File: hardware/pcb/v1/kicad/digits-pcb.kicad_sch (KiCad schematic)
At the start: 19 parts, among them J1 Conn_02x20_Odd_Even, J10 Conn_01x02, J2 Conn_01x03, J3 Barrel_Jack_Switch, J4 Conn_01x07, J5 Conn_01x04, J6 Conn_01x02, J7 Screw_Terminal_01x02, J8 Conn_01x04, J9 Conn_01x03, SW1 SW_Push, U1 LM2596S-5

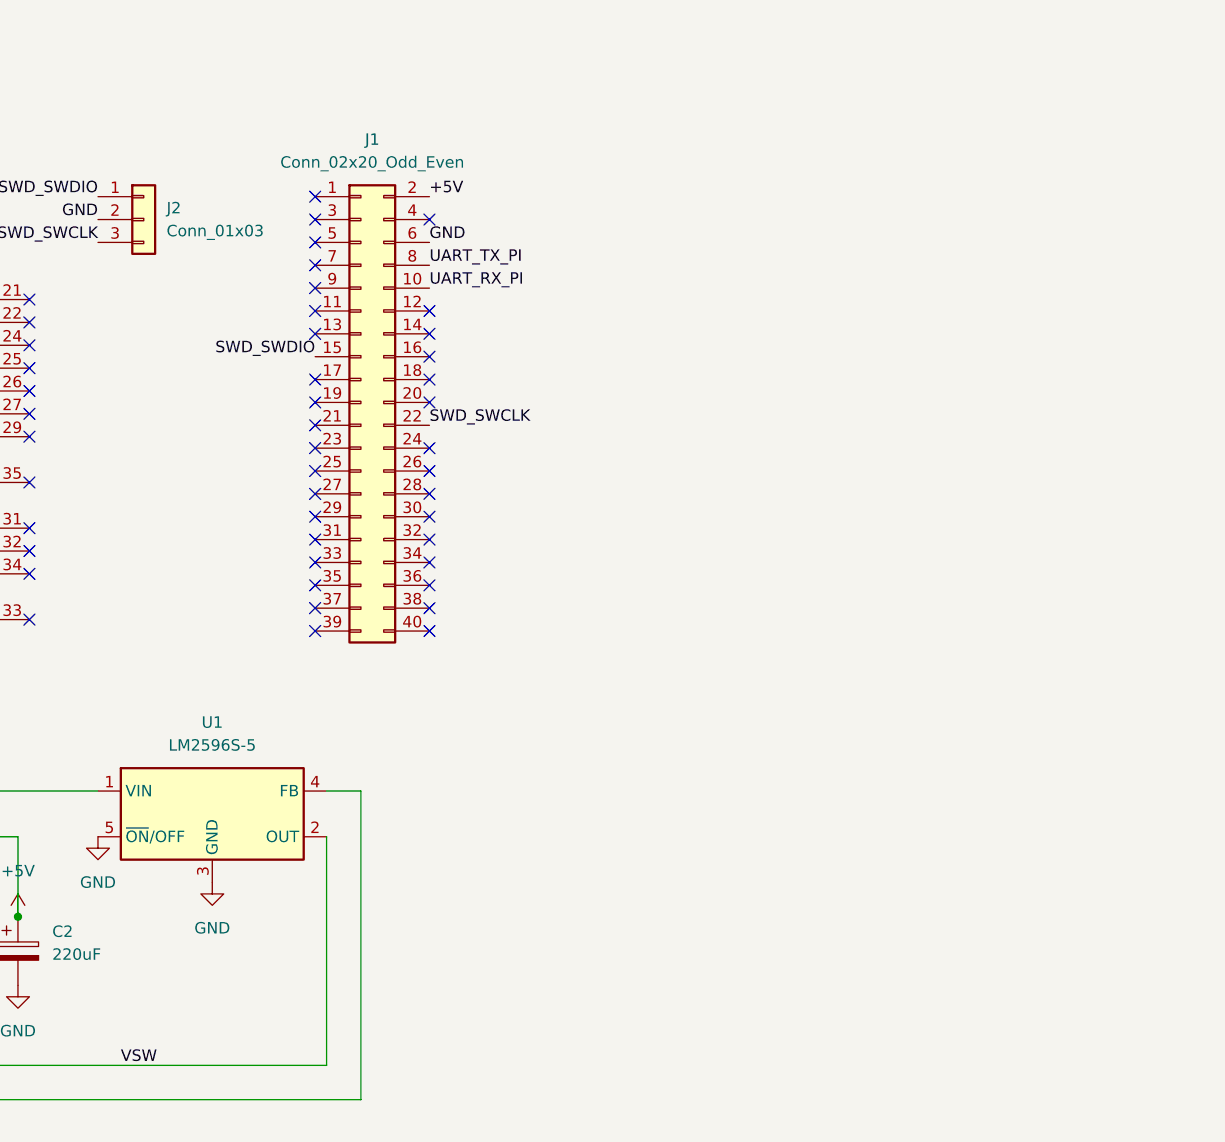
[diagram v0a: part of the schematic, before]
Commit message: feat(hardware): v1.1 design in progress — codec header + audit follow-ups
Schematic (via subagents + manual):
- Add J_CODEC (2x20 female, Conn_02x20_Odd_Even) for the Codec Zero HAT to
  plug into directly via its factory 40-pin receptacle
- Add global labels linking J1 <-> J_CODEC for the 8 audio + power signals:
  CODEC_SDA, CODEC_SCL, CODEC_BCLK, CODEC_WCLK, CODEC_DIN, CODEC_DOUT, plus
  +3V3 and GND
- Add HAT_ID_SD / HAT_ID_SC labels on J1 pins 27/28 and J_CODEC pins 27/28
  so the Pi bootloader can auto-detect the HAT via its on-board EEPROM
- No_connect flags on unused J_CODEC pins

ERRATA.md:
- Annotate v1.1 resolution status for each of the 5 pre-existing errata
  items. #1 (switching node) marked APPLIED; #2-5 marked PENDING for v1.1
- Add introductory note that the design files in this directory are now
  evolving toward v1.1

PCB (WIP):
- Initial placement tweaks; full routing of J_CODEC + resolution of the
  other errata items is in progress
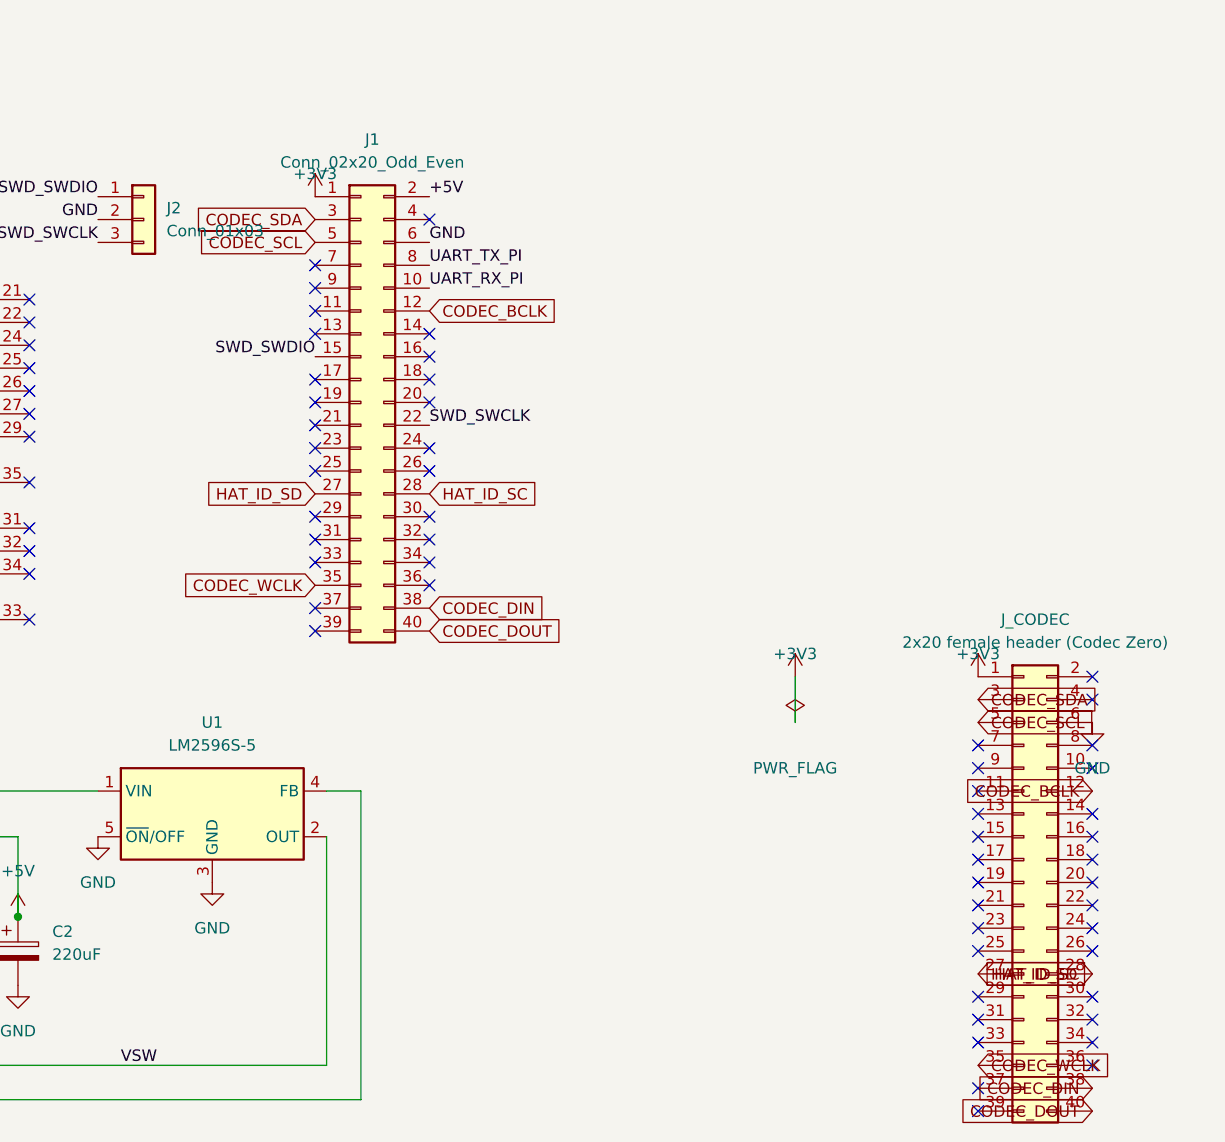
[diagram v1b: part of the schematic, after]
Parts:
- added J_CODEC: 2x20 female header (Codec Zero), Connector_PinHeader_2.54mm:PinHeader_2x20_P2.54mm_Vertical, symbol Connector_Generic:Conn_02x20_Odd_Even
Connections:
- net GND: now also J_CODEC.6 (Pin_6)
- net +3V3: now reaches J1.1 (Pin_1)
- net +3V3: now also J_CODEC.1 (Pin_1)
- net CODEC_BCLK: now reaches J1.12 (Pin_12)
- net CODEC_BCLK: now also J_CODEC.12 (Pin_12)
- net HAT_ID_SD: now reaches J1.27 (Pin_27)
- net HAT_ID_SD: now also J_CODEC.27 (Pin_27)
- net HAT_ID_SC: now reaches J1.28 (Pin_28)
- net HAT_ID_SC: now also J_CODEC.28 (Pin_28)
- net CODEC_SDA: now reaches J1.3 (Pin_3)
- net CODEC_SDA: now also J_CODEC.3 (Pin_3)
- net CODEC_WCLK: now reaches J1.35 (Pin_35)
- net CODEC_WCLK: now also J_CODEC.35 (Pin_35)
- net CODEC_DIN: now reaches J1.38 (Pin_38)
- net CODEC_DIN: now also J_CODEC.38 (Pin_38)
- net CODEC_DOUT: now reaches J1.40 (Pin_40)
- net CODEC_DOUT: now also J_CODEC.40 (Pin_40)
- net CODEC_SCL: now reaches J1.5 (Pin_5)
- net CODEC_SCL: now also J_CODEC.5 (Pin_5)
- no-connect marks 54 -> 75

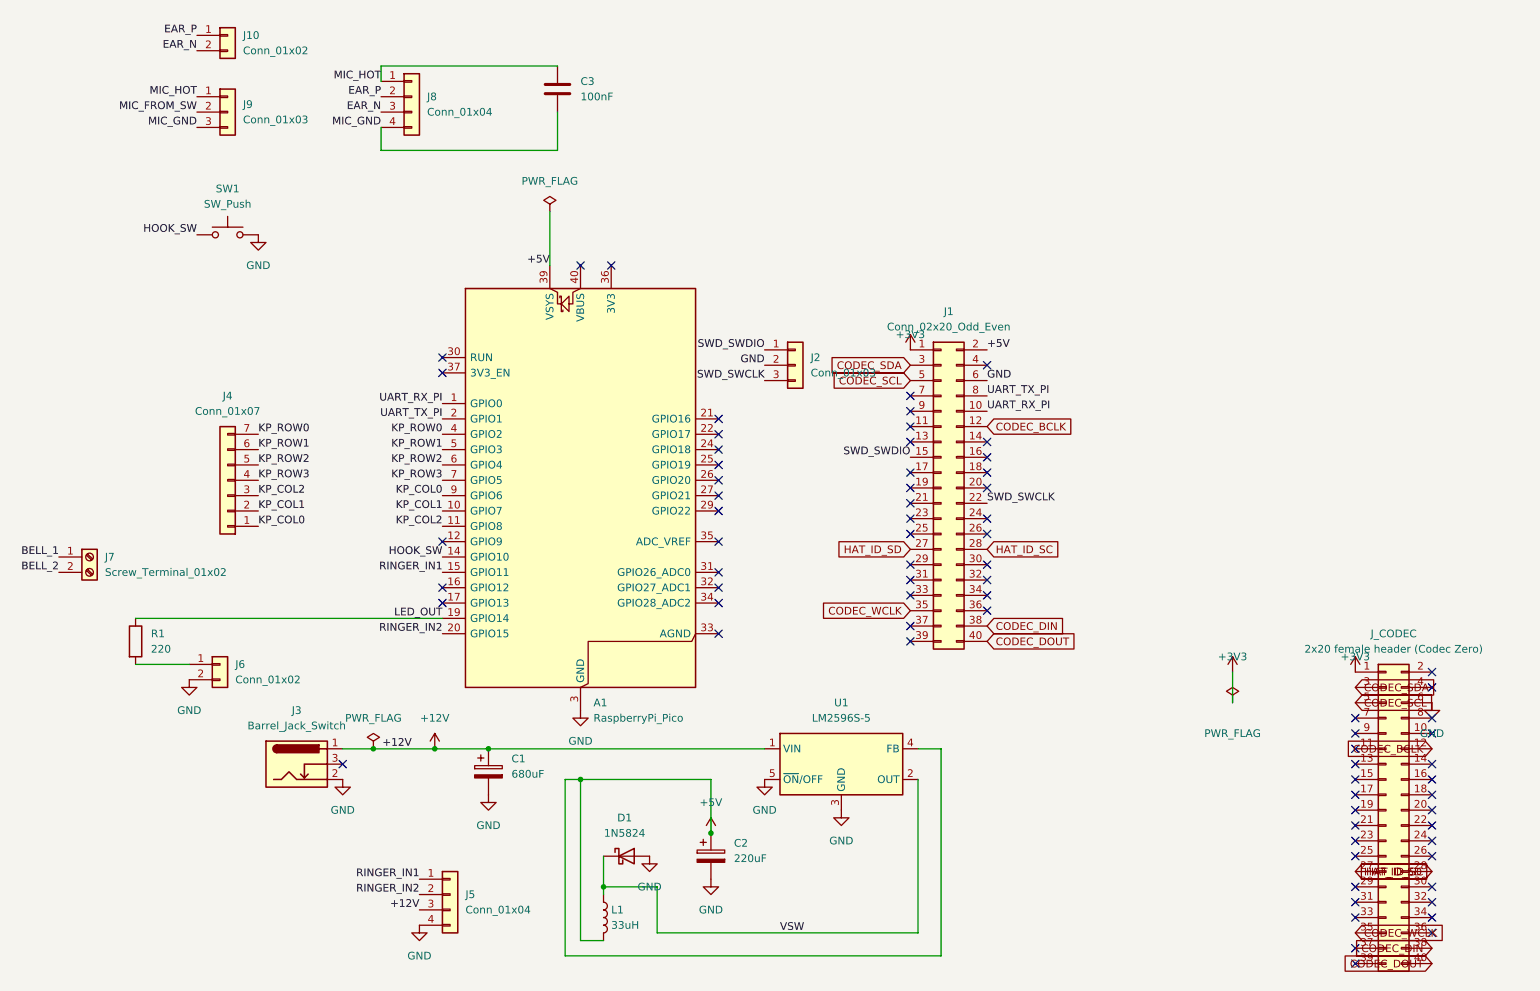
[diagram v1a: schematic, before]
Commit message: chore(hardware): v1.1 WIP checkpoint - codec passthrough, mic jumper, VSW
Schematic (ERC clean):
- All 40 pins of J1 (Pi) and J_CODEC (Codec Zero) tied pin-for-pin via
  global labels for full HAT-style GPIO passthrough
- Wire CODEC_MCLK on pin 7 (was missing - required for TLV320AIC3104
  master clock derived from Pi GPCLK0)
- Add J11 1x2 mic-to-codec jumper (pin 1 = MIC_FROM_SW, pin 2 = MIC_GND);
  mirrors J10 earpiece pattern. Eliminates the v1.0 flying-wire kludge
  from J9 to the Codec Zero mic JST.
- Add 3 mounting hole symbols (MH1/2/3) with markup matching v2 style
- Fix J_CODEC value/description text to read "male" header (footprint
  was always male PinHeader; only the labels were wrong)

PCB (DRC clean with --refill-zones):
- Restore mounting holes at original v1 positions; add schematic-link
  metadata (path/sheetname/sheetfile/units) so KiCad recognizes them
  as schematic-backed components
- Apply errata #1 PCB-side fix: rename Net-(D1-K) to /VSW (sheet-scoped
  label name from schematic) and widen 5 buck switching segments from
  0.25mm to 0.75mm
- Update Power netclass pattern in .kicad_pro from "VSW" to "/VSW" to
  match the slash-prefixed name (per power-integrity audit memory:
  hierarchical net path prefixes silently break unprefixed patterns)

NEXT_STEPS.md added documenting remaining work. Main blocker is
mechanical: the Pi and Codec Zero overlap in the current J1/J_CODEC
orientation. Several errata items still pending. Not ready for fab.
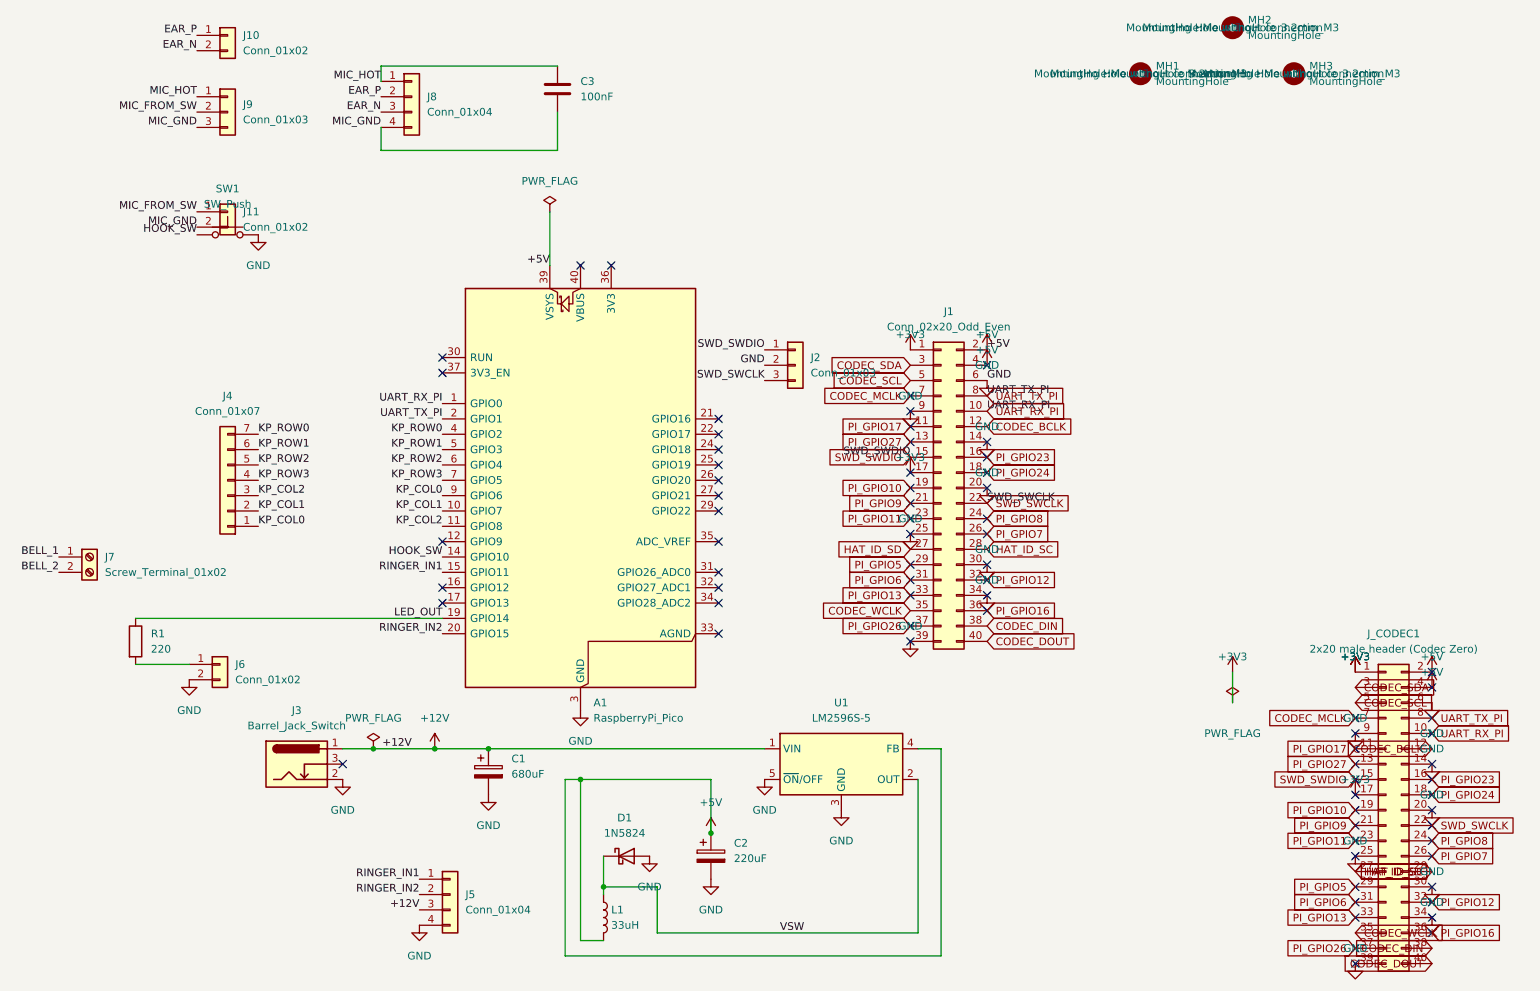
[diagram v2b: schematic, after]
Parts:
- added J11: Conn_01x02, Connector_PinHeader_2.54mm:PinHeader_1x02_P2.54mm_Vertical, symbol Connector_Generic:Conn_01x02
- added MH1, MH2, MH3: MountingHole, MountingHole:MountingHole_3.2mm_M3, symbol Mechanical:MountingHole
- J_CODEC1: renamed from J_CODEC; value 2x20 female header (Codec Zero) -> 2x20 male header (Codec Zero)
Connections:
- net +3V3: now also J1.17 (Pin_17), J_CODEC1.17 (Pin_17)
- net +5V: now also J1.4 (Pin_4), J_CODEC1.2 (Pin_2), J_CODEC1.4 (Pin_4)
- net GND: now also J1.14 (Pin_14), J1.20 (Pin_20), J1.25 (Pin_25), J1.30 (Pin_30), J1.34 (Pin_34), J1.39 (Pin_39), J1.9 (Pin_9), J_CODEC1.14 (Pin_14), J_CODEC1.20 (Pin_20), J_CODEC1.25 (Pin_25), J_CODEC1.30 (Pin_30), J_CODEC1.34 (Pin_34), J_CODEC1.39 (Pin_39), J_CODEC1.9 (Pin_9)
- net MIC_FROM_SW: now also J11.1 (Pin_1)
- net MIC_GND: now also J11.2 (Pin_2)
- net SWD_SWCLK: now also J_CODEC1.22 (Pin_22)
- net SWD_SWDIO: now also J_CODEC1.15 (Pin_15)
- net UART_RX_PI: now also J_CODEC1.10 (Pin_10)
- net UART_TX_PI: now also J_CODEC1.8 (Pin_8)
- net PI_GPIO17: now reaches J1.11 (Pin_11)
- net PI_GPIO17: now also J_CODEC1.11 (Pin_11)
- net PI_GPIO27: now reaches J1.13 (Pin_13)
- net PI_GPIO27: now also J_CODEC1.13 (Pin_13)
- net PI_GPIO23: now reaches J1.16 (Pin_16)
- net PI_GPIO23: now also J_CODEC1.16 (Pin_16)
- net PI_GPIO24: now reaches J1.18 (Pin_18)
- net PI_GPIO24: now also J_CODEC1.18 (Pin_18)
- net PI_GPIO10: now reaches J1.19 (Pin_19)
- net PI_GPIO10: now also J_CODEC1.19 (Pin_19)
- net PI_GPIO9: now reaches J1.21 (Pin_21)
- net PI_GPIO9: now also J_CODEC1.21 (Pin_21)
- net PI_GPIO11: now reaches J1.23 (Pin_23)
- net PI_GPIO11: now also J_CODEC1.23 (Pin_23)
- net PI_GPIO8: now reaches J1.24 (Pin_24)
- net PI_GPIO8: now also J_CODEC1.24 (Pin_24)
- net PI_GPIO7: now reaches J1.26 (Pin_26)
- net PI_GPIO7: now also J_CODEC1.26 (Pin_26)
- net PI_GPIO5: now reaches J1.29 (Pin_29)
- net PI_GPIO5: now also J_CODEC1.29 (Pin_29)
- net PI_GPIO6: now reaches J1.31 (Pin_31)
- net PI_GPIO6: now also J_CODEC1.31 (Pin_31)
- net PI_GPIO12: now reaches J1.32 (Pin_32)
- net PI_GPIO12: now also J_CODEC1.32 (Pin_32)
- net PI_GPIO13: now reaches J1.33 (Pin_33)
- net PI_GPIO13: now also J_CODEC1.33 (Pin_33)
- net PI_GPIO16: now reaches J1.36 (Pin_36)
- net PI_GPIO16: now also J_CODEC1.36 (Pin_36)
- net PI_GPIO26: now reaches J1.37 (Pin_37)
- net PI_GPIO26: now also J_CODEC1.37 (Pin_37)
- net CODEC_MCLK: now reaches J1.7 (Pin_7)
- net CODEC_MCLK: now also J_CODEC1.7 (Pin_7)
